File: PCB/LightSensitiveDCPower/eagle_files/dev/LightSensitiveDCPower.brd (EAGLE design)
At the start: 12 x 31.3 mm, 4 parts

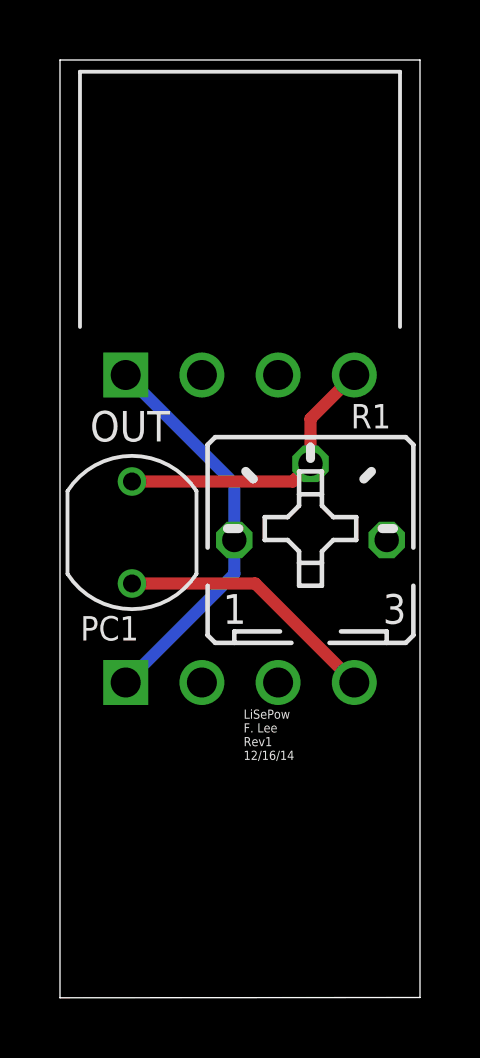
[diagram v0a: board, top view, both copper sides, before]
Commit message: LiSensiPow actually works now
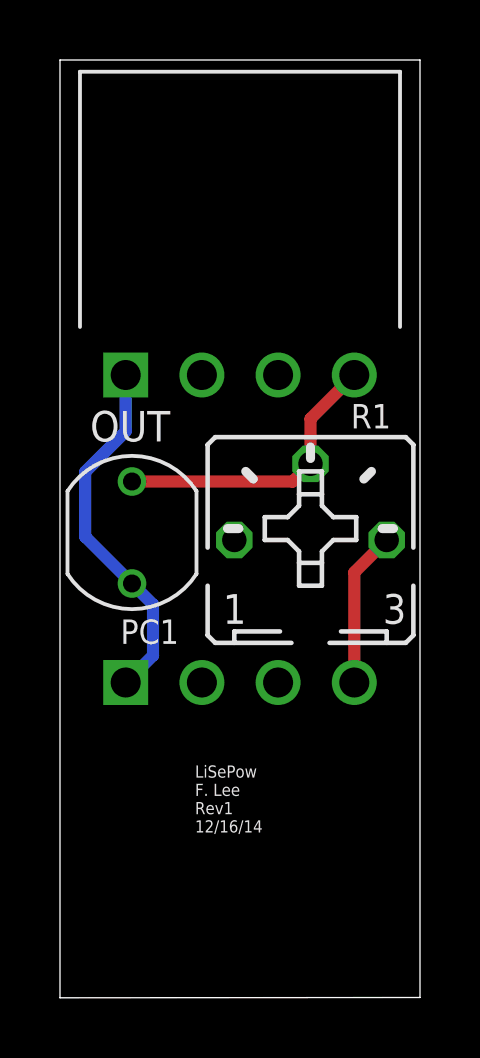
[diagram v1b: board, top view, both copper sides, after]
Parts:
- turned PC1 to 0 degrees
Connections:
- removed net N$2: IN.P$4, PC1.1
- new net N$3: IN.P$4, R1.E
- net N$1: now also PC1.2; no longer R1.A
- net N$4: now also PC1.1; no longer PC1.2
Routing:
- net N$2: track 8.78 -> 0.00 mm
- net N$3: track 0.00 -> 5.20 mm
- net N$1: track 13.2 -> 12.1 mm
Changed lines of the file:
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@@
 <wire x1="12" y1="31.25" x2="0" y2="31.25" width="0" layer="20"/>
 <wire x1="0" y1="31.25" x2="0" y2="-0.01" width="0" layer="20"/>
-<text x="6.12" y="7.92" size="0.3048" layer="25">LiSePow
+<text x="4.5" y="5.5" size="0.4064" layer="21">LiSePow
 F. Lee
 Rev1
@@
 </autorouter>
 <elements>
-<element name="PC1" library="freddyLibr" package="PHOTOCELL_CERAMIC" value="" x="2.4" y="15.5" smashed="yes" rot="R180">
-<attribute name="NAME" x="0.68" y="11.9" size="0.8128" layer="25"/>
+<element name="PC1" library="freddyLibr" package="PHOTOCELL_CERAMIC" value="" x="2.4" y="15.5" smashed="yes">
+<attribute name="NAME" x="3.96" y="12.6" size="0.8128" layer="25" rot="R180"/>
 </element>
 <element name="R1" library="pot" package="B25P" value="" x="8.35" y="15.25" smashed="yes">
@@
 <signals>
 <signal name="N$1">
-<contactref element="R1" pad="A"/>
 <contactref element="IN" pad="P$1"/>
+<contactref element="PC1" pad="2"/>
 <contactref element="OUT" pad="P$1"/>
-<wire x1="2.19" y1="10.5" x2="5.81" y2="14.12" width="0.4064" layer="16"/>
-<wire x1="5.81" y1="14.12" x2="5.81" y2="15.25" width="0.4064" layer="16"/>
-<wire x1="5.81" y1="15.25" x2="5.81" y2="17.13" width="0.4064" layer="16"/>
-<wire x1="5.81" y1="17.13" x2="2.19" y2="20.75" width="0.4064" layer="16"/>
+<wire x1="2.19" y1="20.75" x2="2.19" y2="18.87" width="0.4064" layer="16"/>
+<wire x1="2.19" y1="18.87" x2="0.84" y2="17.52" width="0.4064" layer="16"/>
+<wire x1="0.84" y1="17.52" x2="0.84" y2="15.36" width="0.4064" layer="16"/>
+<wire x1="0.84" y1="15.36" x2="2.4" y2="13.8" width="0.4064" layer="16"/>
+<wire x1="2.19" y1="10.5" x2="2.2" y2="10.5" width="0.4064" layer="16"/>
+<wire x1="2.2" y1="10.5" x2="3.1" y2="11.4" width="0.4064" layer="16"/>
+<wire x1="3.1" y1="11.4" x2="3.1" y2="13.1" width="0.4064" layer="16"/>
+<wire x1="3.1" y1="13.1" x2="2.4" y2="13.8" width="0.4064" layer="16"/>
 </signal>
-<signal name="N$2">
+<signal name="N$3">
 <contactref element="IN" pad="P$4"/>
-<contactref element="PC1" pad="1"/>
-<wire x1="2.4" y1="13.8" x2="6.51" y2="13.8" width="0.4064" layer="1"/>
-<wire x1="6.51" y1="13.8" x2="9.81" y2="10.5" width="0.4064" layer="1"/>
+<contactref element="R1" pad="E"/>
+<wire x1="9.81" y1="10.5" x2="9.81" y2="14.17" width="0.4064" layer="1"/>
+<wire x1="9.81" y1="14.17" x2="10.89" y2="15.25" width="0.4064" layer="1"/>
 </signal>
 <signal name="N$4">
 <contactref element="R1" pad="S"/>
-<contactref element="PC1" pad="2"/>
 <contactref element="OUT" pad="P$4"/>
+<contactref element="PC1" pad="1"/>
 <wire x1="8.35" y1="17.79" x2="8.35" y2="19.29" width="0.4064" layer="1"/>
 <wire x1="8.35" y1="19.29" x2="9.81" y2="20.75" width="0.4064" layer="1"/>
